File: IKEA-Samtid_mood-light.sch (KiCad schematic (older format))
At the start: 15 parts, among them IC1 ATMEGA168PA-M, P1 FTDI, P2 POWER, P3 MCU-Board, SW1 MODE, SW2 +/-, X1 CSTCE16M0V53-R0

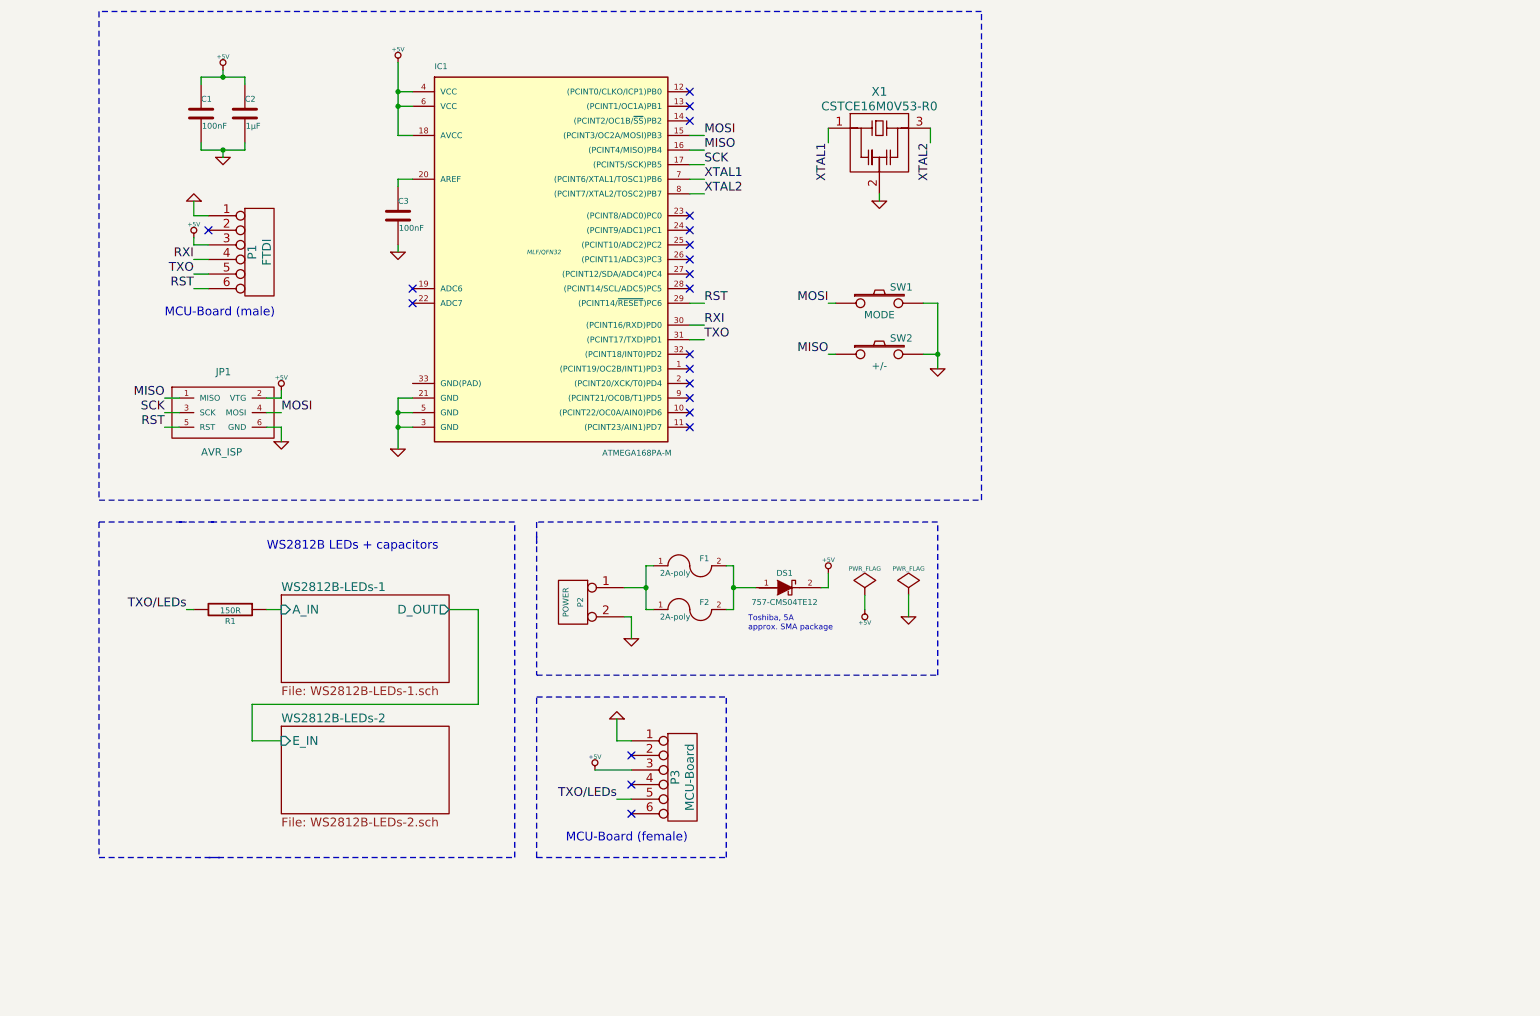
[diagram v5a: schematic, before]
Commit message: Using board-to-board connectors (micro-Match).
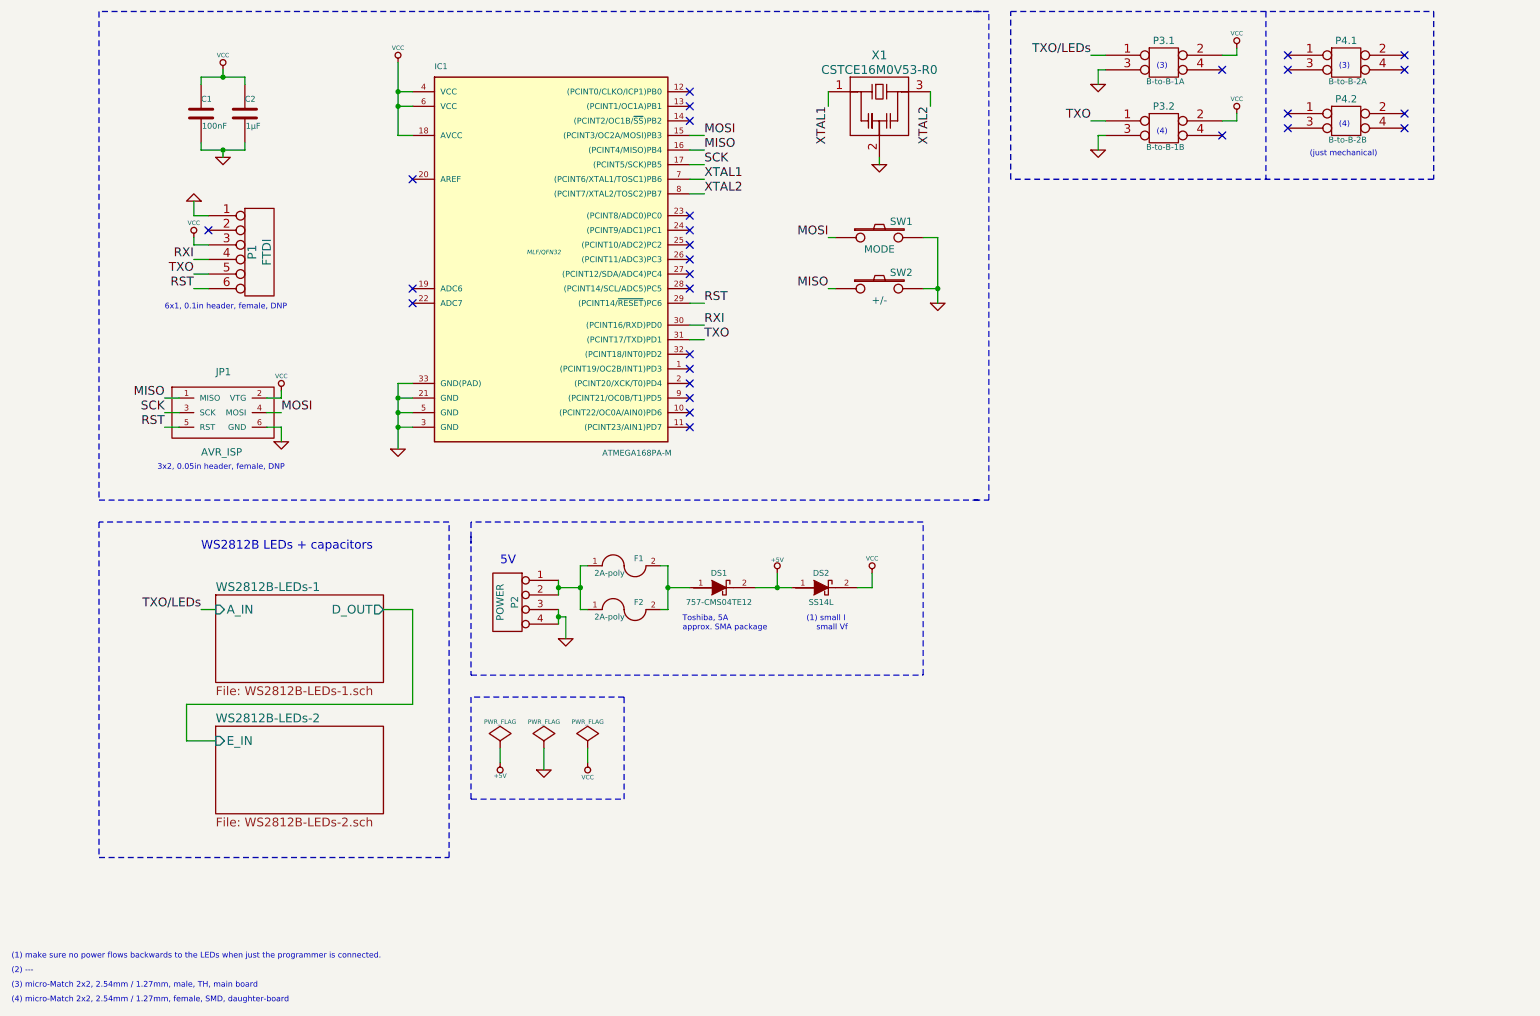
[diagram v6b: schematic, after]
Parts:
- removed C3: 100nF, symbol C
- removed P2: POWER, symbol CONN_2
- removed P3: MCU-Board, symbol CONN_6
- removed R1: 150R, symbol R
- added DS2: SS14L, symbol DIODESCH
- added P2: POWER, symbol CONN_4
- added P3.1: B-to-B-1A, symbol CONN_2X2
- added P3.2: B-to-B-1B, symbol CONN_2X2
- added P4.1: B-to-B-2A, symbol CONN_2X2
- added P4.2: B-to-B-2B, symbol CONN_2X2
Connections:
- net +5V: now also DS2.1 (A); no longer C1.1, C2.1, IC1.18 (AVCC), IC1.4 (VCC), IC1.6 (VCC), JP1.2 (VTG), P1.3
- net GND: now also IC1.33 (GND(PAD)), P2.3 (P3), P2.4 (P4), P3.1.3, P3.2.3
- net TXO: now also P3.2.1
- net TXO/LEDs: now also P3.1.1
- net at F1.1, F2.1: now also P2.1 (P1), P2.2 (P2)
- new net VCC: C1.1, C2.1, DS2.2 (C), IC1.18 (AVCC), IC1.4 (VCC), IC1.6 (VCC), JP1.2 (VTG), P1.3, P3.1.2, P3.2.2
- no-connect marks 21 -> 29
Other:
- note added: "(1) make sure no power flows backwards to the LEDs when just the programmer is connected."
- note added: "(1) small I\n small Vf"
- note added: "(2) ---"
- note added: "(3)"
- note added: "(3) micro-Match 2x2, 2.54mm / 1.27mm, male, TH, main board"
- note added: "(4)"
- note added: "(4) micro-Match 2x2, 2.54mm / 1.27mm, female, SMD, daughter-board"
- note added: "(just mechanical)"
- note added: "3x2, 0.05in header, female, DNP"
- note added: "5V"
- note added: "6x1, 0.1in header, female, DNP"
- note removed: "MCU-Board (female)"
- note removed: "MCU-Board (male)"
- moved on the sheet: DS1, F1, F2, SW1, SW2, X1

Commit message: Getting lost in hirarchical schematic sheets...
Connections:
- net GND renamed GND.B
- net GND.B: no longer P2.3 (P3), P2.4 (P4), P3.1.3
- net VCC renamed VCC.B
- net VCC.B: no longer DS2.2 (C), P3.1.2
- new net GND.A: P2.3 (P3), P2.4 (P4), P3.1.3
- new net VCC.A: DS2.2 (C), P3.1.2
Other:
- moved on the sheet: P3.1, P3.2, P4.1, P4.2, SW1, SW2

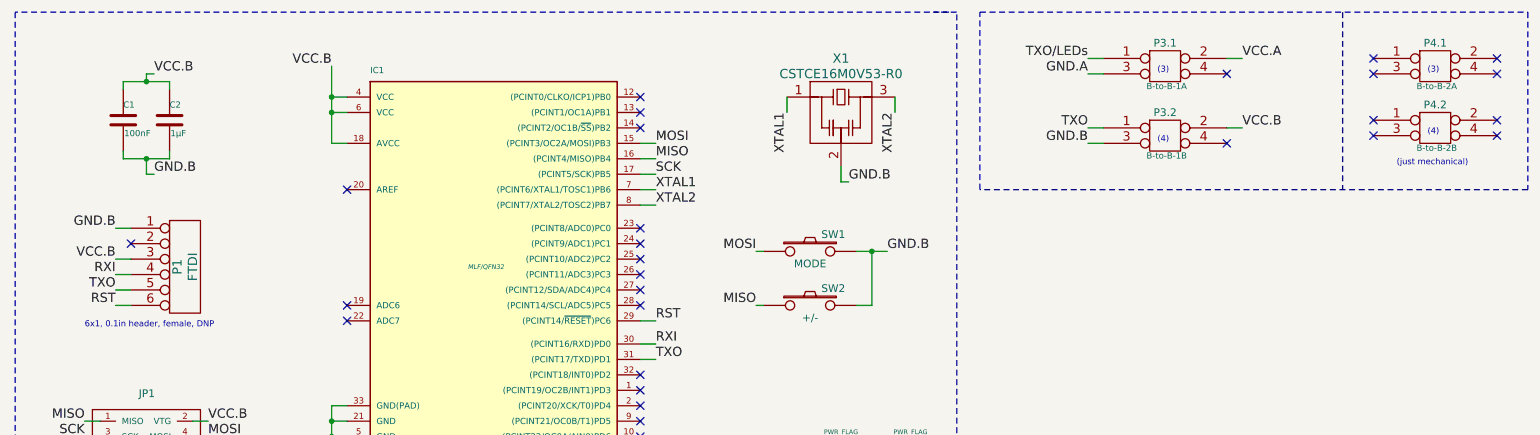
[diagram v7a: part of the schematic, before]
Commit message: Hirarchical schem. sheets have 'interesting' effects on net-names.
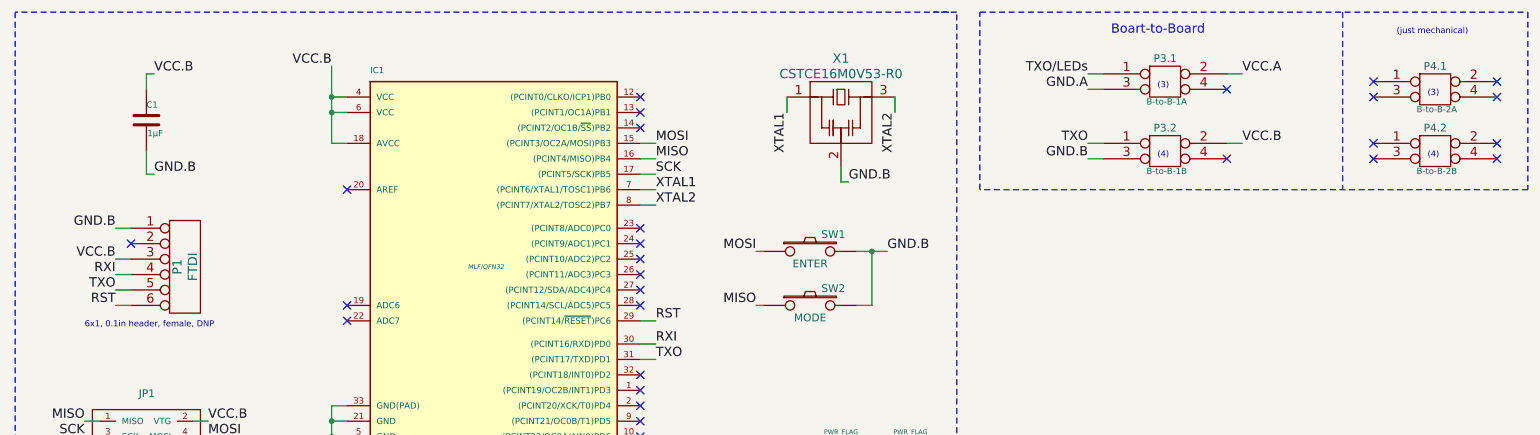
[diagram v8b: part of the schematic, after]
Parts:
- removed C2: 1µF, symbol C
- C1: value 100nF -> 1µF
- SW1: value MODE -> ENTER
- SW2: value +/- -> MODE
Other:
- note added: "Boart-to-Board"
- moved on the sheet: C1, P3.1, P3.2, P4.1, P4.2
